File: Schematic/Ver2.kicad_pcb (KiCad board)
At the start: 2 copper layers, 32 x 22 mm, 21 parts, among them IC1 ATMEGA328P-A, P1 PROG, P2 Power, P3 OLED, P4 DBG, SW1 SW_Push, U1 L78L05ABUTR

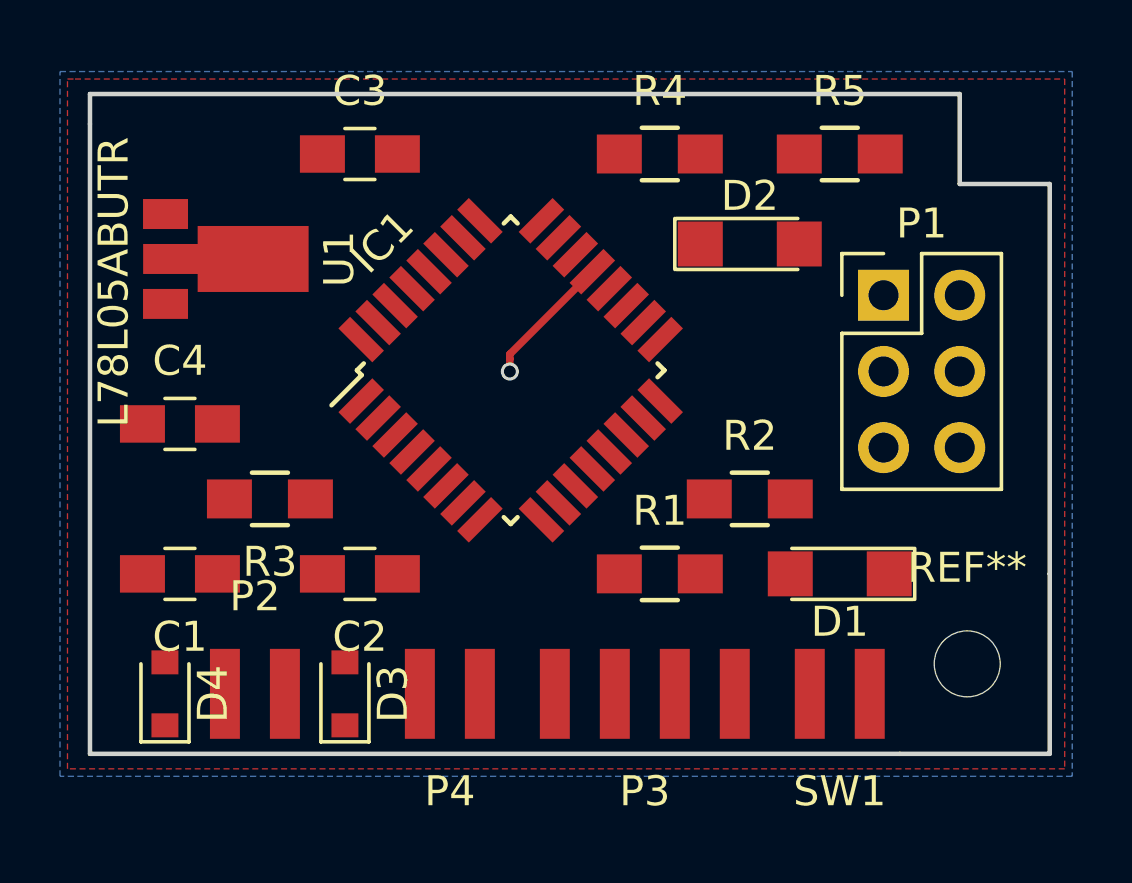
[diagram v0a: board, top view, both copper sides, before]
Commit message: Created a Atmel project and started with initcode
Got UART and OLED display to work. Also created a welcome message
screen.
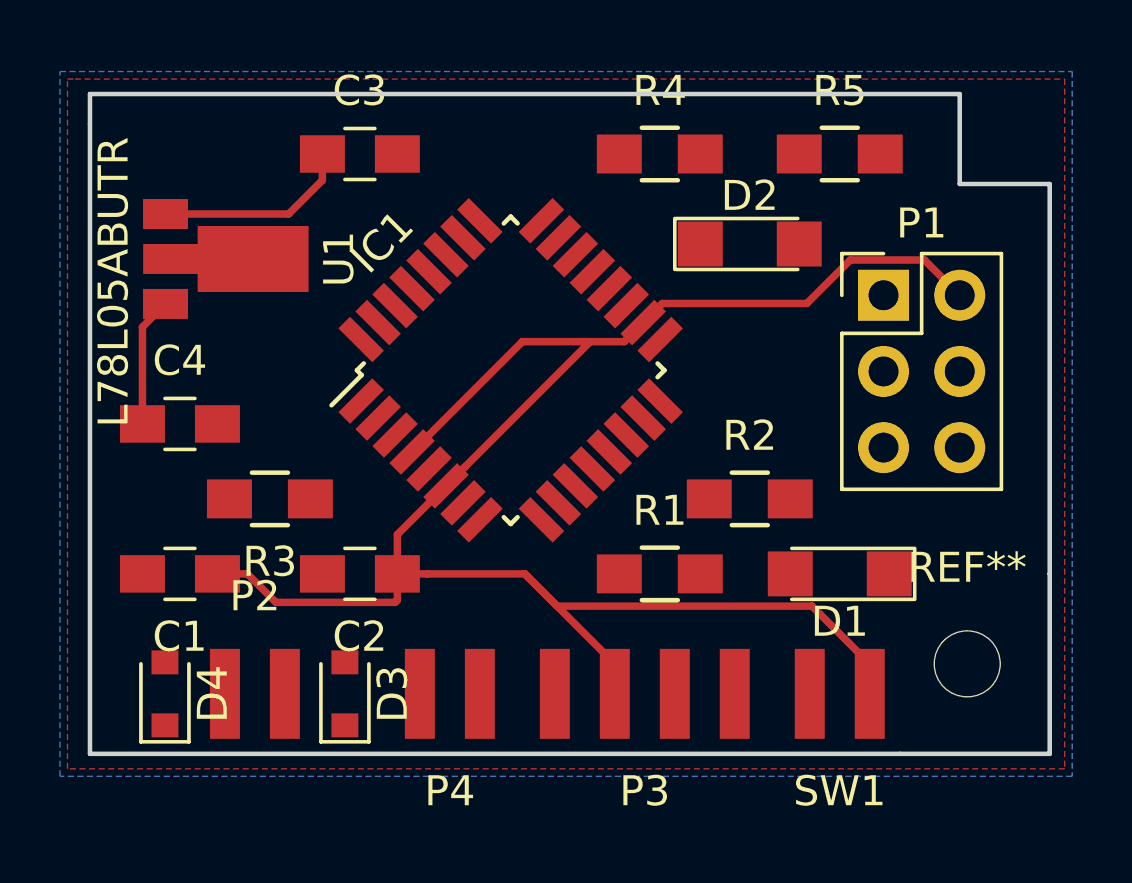
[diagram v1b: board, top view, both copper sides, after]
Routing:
- net /5V: track 0.00 -> 68.9 mm
- net GND: track 4.47 -> 0.00 mm, vias 1 -> 0
- net Net-(C4-Pad1): track 0.00 -> 4.32 mm
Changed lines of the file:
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@@
     (thickness 1.6)
     (drawings 9)
-    (tracks 4)
+    (tracks 31)
     (zones 0)
     (modules 21)
@@
   (gr_line (start 156 129) (end 156 108) (layer Edge.Cuts) (width 0.15))
   (gr_line (start 183 129) (end 156 129) (layer Edge.Cuts) (width 0.15))
-  (segment (start 169.999222 115.828973) (end 169.999222 116.253237) (width 0.25) (layer F.Cu) (net 2))
-  (segment (start 169.999222 115.674684) (end 169.999222 115.828973) (width 0.25) (layer F.Cu) (net 2))
-  (segment (start 172.75 112.923906) (end 169.999222 115.674684) (width 0.25) (layer F.Cu) (net 2))
-  (via (at 169.999222 116.253237) (size 0.6) (drill 0.4) (layers F.Cu B.Cu) (net 2))
+  (segment (start 166.739592 118.934314) (end 170.416548 115.257358) (width 0.25) (layer F.Cu) (net 1))
+  (segment (start 170.416548 115.257358) (end 172.67929 115.257358) (width 0.25) (layer F.Cu) (net 1))
+  (segment (start 174.447056 114.620963) (end 173.810661 115.257358) (width 0.25) (layer F.Cu) (net 1))
+  (segment (start 168.507358 119.42929) (end 167.870963 120.065685) (width 0.25) (layer F.Cu) (net 1))
+  (segment (start 173.810661 115.257358) (end 172.67929 115.257358) (width 0.25) (layer F.Cu) (net 1))
+  (segment (start 172.67929 115.257358) (end 168.507358 119.42929) (width 0.25) (layer F.Cu) (net 1))
+  (segment (start 158.519 111.001) (end 162.624 111.001) (width 0.25) (layer F.Cu) (net 1))
+  (segment (start 162.624 111.001) (end 163.75 109.875) (width 0.25) (layer F.Cu) (net 1))
+  (segment (start 163.75 109.875) (end 163.75 109) (width 0.25) (layer F.Cu) (net 1))
+  (segment (start 185 113.71) (end 183.824999 112.534999) (width 0.25) (layer F.Cu) (net 1))
+  (segment (start 181.349999 112.534999) (end 179.90043 113.984568) (width 0.25) (layer F.Cu) (net 1))
+  (segment (start 183.824999 112.534999) (end 181.349999 112.534999) (width 0.25) (layer F.Cu) (net 1))
+  (segment (start 179.90043 113.984568) (end 175.083451 113.984568) (width 0.25) (layer F.Cu) (net 1))
+  (segment (start 175.083451 113.984568) (end 174.447056 114.620963) (width 0.25) (layer F.Cu) (net 1))
+  (segment (start 166.25 123) (end 166.25 123.875) (width 0.25) (layer F.Cu) (net 1))
+  (segment (start 166.25 123.875) (end 166.174999 123.950001) (width 0.25) (layer F.Cu) (net 1))
+  (segment (start 166.174999 123.950001) (end 162.200001 123.950001) (width 0.25) (layer F.Cu) (net 1))
+  (segment (start 162.200001 123.950001) (end 161.25 123) (width 0.25) (layer F.Cu) (net 1))
+  (segment (start 161.25 123) (end 160.25 123) (width 0.25) (layer F.Cu) (net 1))
+  (segment (start 182 127) (end 182 126) (width 0.25) (layer F.Cu) (net 1))
+  (segment (start 182 126) (end 180.075001 124.075001) (width 0.25) (layer F.Cu) (net 1))
+  (segment (start 180.075001 124.075001) (end 171.575001 124.075001) (width 0.25) (layer F.Cu) (net 1))
+  (segment (start 171.575001 124.075001) (end 170.5 123) (width 0.25) (layer F.Cu) (net 1))
+  (segment (start 173.5 127) (end 173.5 126) (width 0.25) (layer F.Cu) (net 1))
+  (segment (start 173.5 126) (end 170.5 123) (width 0.25) (layer F.Cu) (net 1))
+  (segment (start 170.5 123) (end 167.25 123) (width 0.25) (layer F.Cu) (net 1))
+  (segment (start 167.25 123) (end 166.25 123) (width 0.25) (layer F.Cu) (net 1))
+  (segment (start 167.870963 120.065685) (end 166.25 121.686648) (width 0.25) (layer F.Cu) (net 1))
+  (segment (start 166.25 121.686648) (end 166.25 123) (width 0.25) (layer F.Cu) (net 1))
+  (segment (start 157.75 118) (end 157.75 114.768) (width 0.25) (layer F.Cu) (net 3))
+  (segment (start 157.75 114.768) (end 158.519 113.999) (width 0.25) (layer F.Cu) (net 3))
   (zone (net 2) (net_name GND) (layer F.Cu) (hatch edge 0.508)
     (connect_pads (clearance 0.13))
     (min_thickness 0.13)
-    (fill yes (arc_segments 16) (thermal_gap 0.508) (thermal_bridge_width 0.508))
+    (fill (arc_segments 16) (thermal_gap 0.508) (thermal_bridge_width 0.508))
     (polygon
       (pts
@@
     (connect_pads (clearance 0.508))
     (min_thickness 0.254)
-    (fill yes (arc_segments 16) (thermal_gap 0.508) (thermal_bridge_width 0.508))
+    (fill (arc_segments 16) (thermal_gap 0.508) (thermal_bridge_width 0.508))
     (polygon
       (pts

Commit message: Added the tracks and completed the design
ordered the cars form OSH park
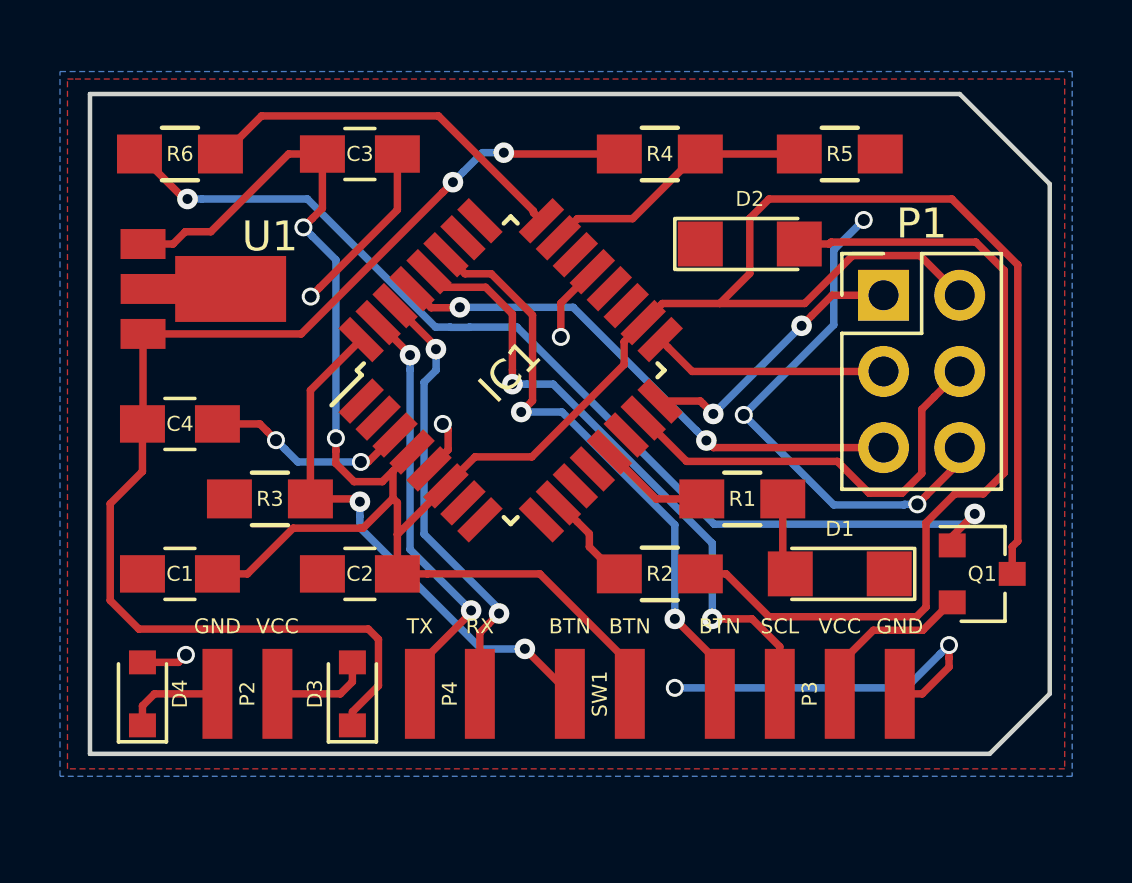
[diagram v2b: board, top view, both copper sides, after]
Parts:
- removed REF**: MountingHole_2.2mm_M2, Mounting_Holes:MountingHole_2.2mm_M2
- added Q1: 2N7002, TO_SOT_Packages_SMD:SOT-23, F.Cu at (185.8, 123.0)
- added R6: R, Resistors_SMD:R_0805_HandSoldering, F.Cu at (159.0, 109.0)
- moved SW1 8.00 mm to (173.0, 127.0)
- moved P3 5.50 mm to (180.0, 127.0), turned to 180 degrees
- moved R2 3.91 mm to (175.0, 123.0)
- moved R1 3.72 mm to (177.8, 120.5)
- moved U1 1.25 mm to (159.8, 113.5)
- moved D4 0.75 mm to (157.8, 127.0)
- moved D3 0.25 mm to (164.8, 127.0)
- moved P2 0.25 mm to (161.2, 127.0)
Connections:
- IC1 pad 24: (no net) -> /OLED_ON
- P3 pad 2: /5V -> Net-(P3-Pad2)
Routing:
- net GND: track 0.00 -> 48.9 mm, vias 0 -> 11
- net Net-(C4-Pad1): track 4.32 -> 40.7 mm, vias 0 -> 2
- net Net-(Q1-Pad1): track 0.00 -> 34.5 mm, vias 0 -> 2
- net Net-(D2-Pad2): track 0.00 -> 28.4 mm
- net /OLED_SCL: track 0.00 -> 21.3 mm, vias 0 -> 2
- net /5V: track 68.9 -> 89.2 mm, vias 0 -> 2
- net /OLED_SDA: track 0.00 -> 20.0 mm, vias 0 -> 2
- net /RESET: track 0.00 -> 17.9 mm, vias 0 -> 2
- net Net-(IC1-Pad32): track 0.00 -> 17.9 mm, vias 0 -> 2
- net /DBG_RX: track 0.00 -> 15.0 mm, vias 0 -> 2
- net /MOSI: track 0.00 -> 14.5 mm
- net /DBG_TX: track 0.00 -> 14.4 mm, vias 0 -> 2
- net /OLED_ON: track 0.00 -> 12.7 mm
- net /MISO: track 0.00 -> 9.26 mm, vias 0 -> 2
- net /VSENSE: track 0.00 -> 9.19 mm
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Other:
- outline, holes or cut-outs redrawn
- rule trace_min: 0.2 -> 0.13
- rule via_min_drill: 0.3 -> 0.254
- rule via_min_size: 0.4 -> 0.4572
- board text added: "BTN"
- board text added: "GND"
- board text added: "RX"
- board text added: "SCL"
- board text added: "TX"
- board text added: "V-Sense"
- board text added: "VCC"
- board text added: "by: Team Embedded"
